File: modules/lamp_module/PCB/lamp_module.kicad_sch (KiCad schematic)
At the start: 36 parts, among them J1 Screw_Terminal_01x02, J2 Screw_Terminal_01x02, J3 Conn_01x06_Socket, K1 12V 5A, K2 12V 5A, Q1 2N7002H, Q2 2N7002H, U1 AMS1117-3.3, U2 ESP-12E, U4 PC817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

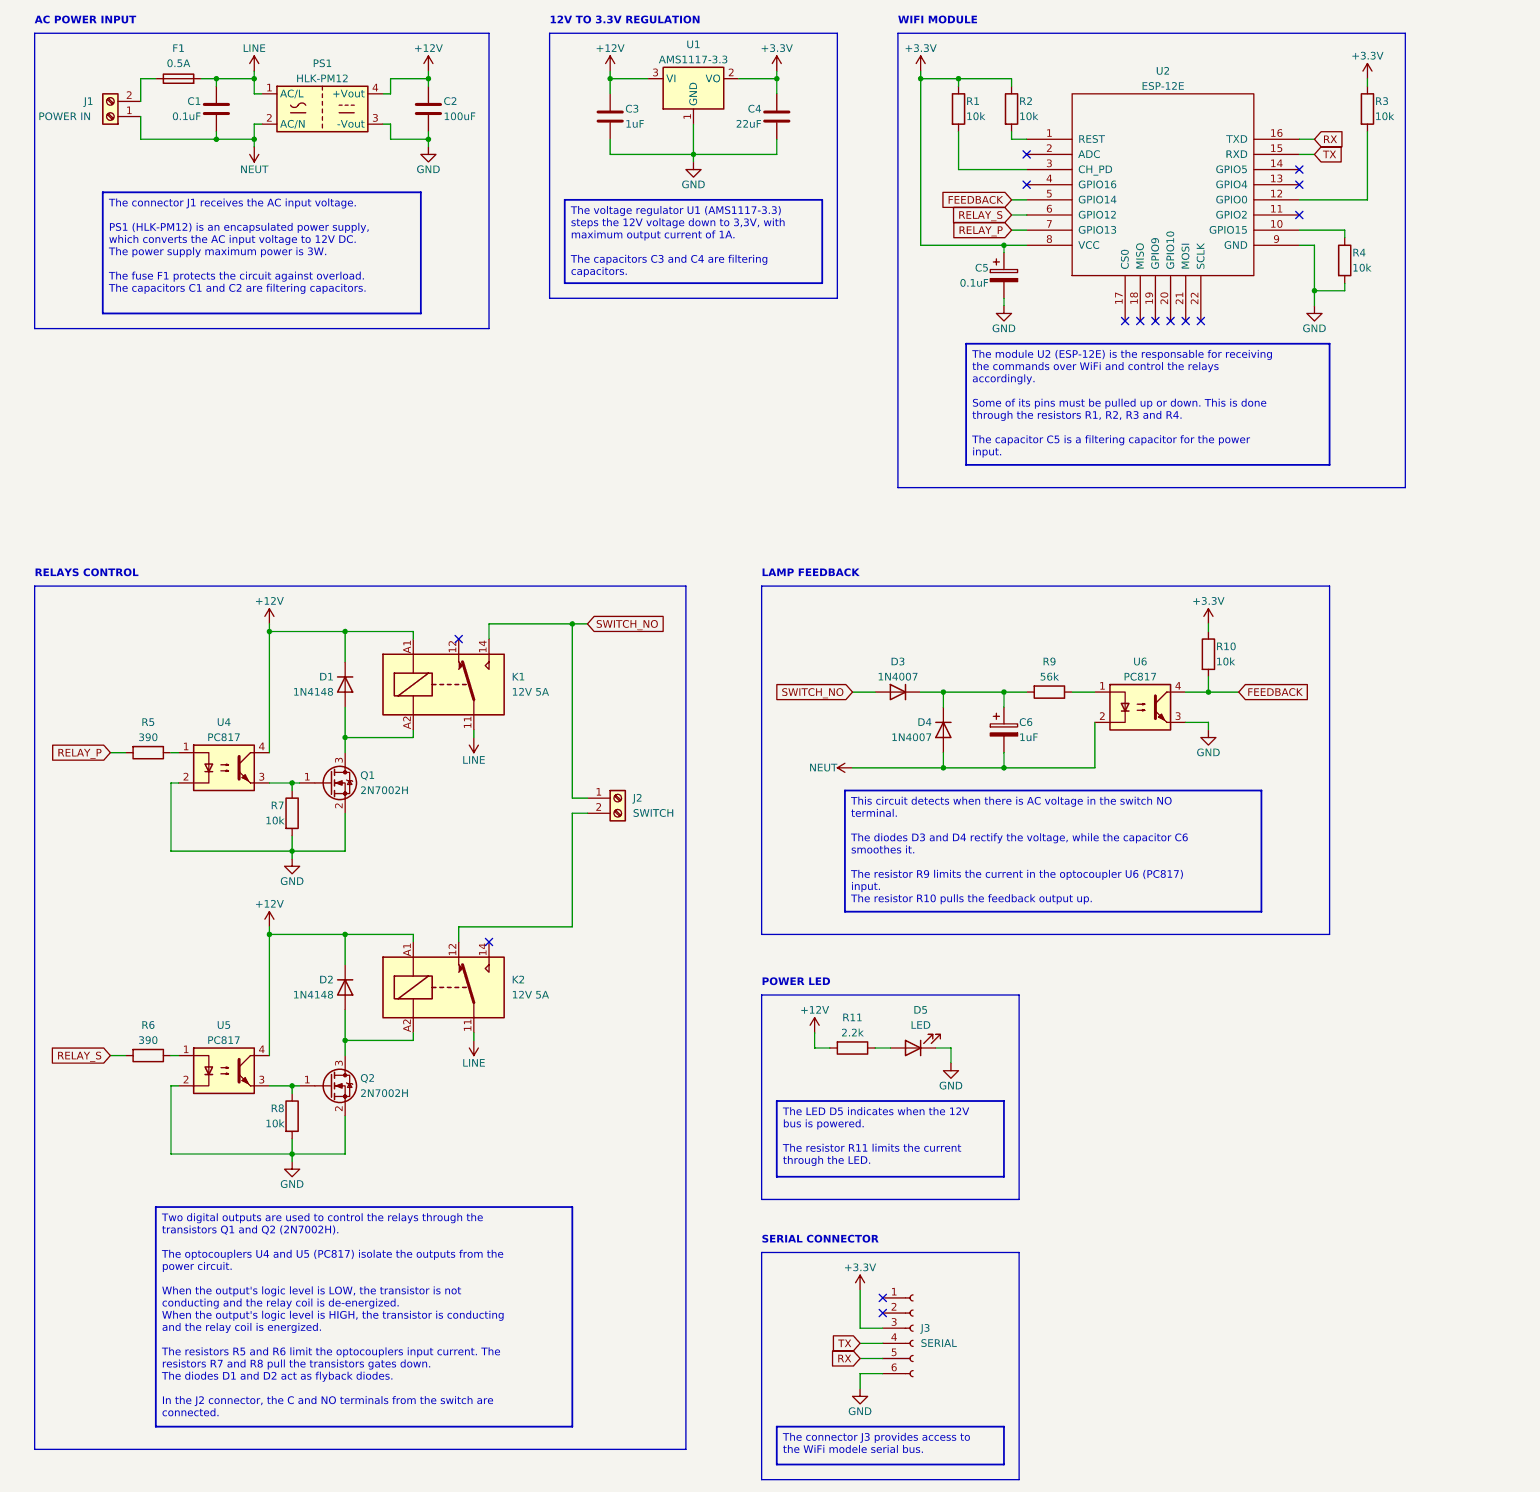
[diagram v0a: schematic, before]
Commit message: PCB simplified and improved
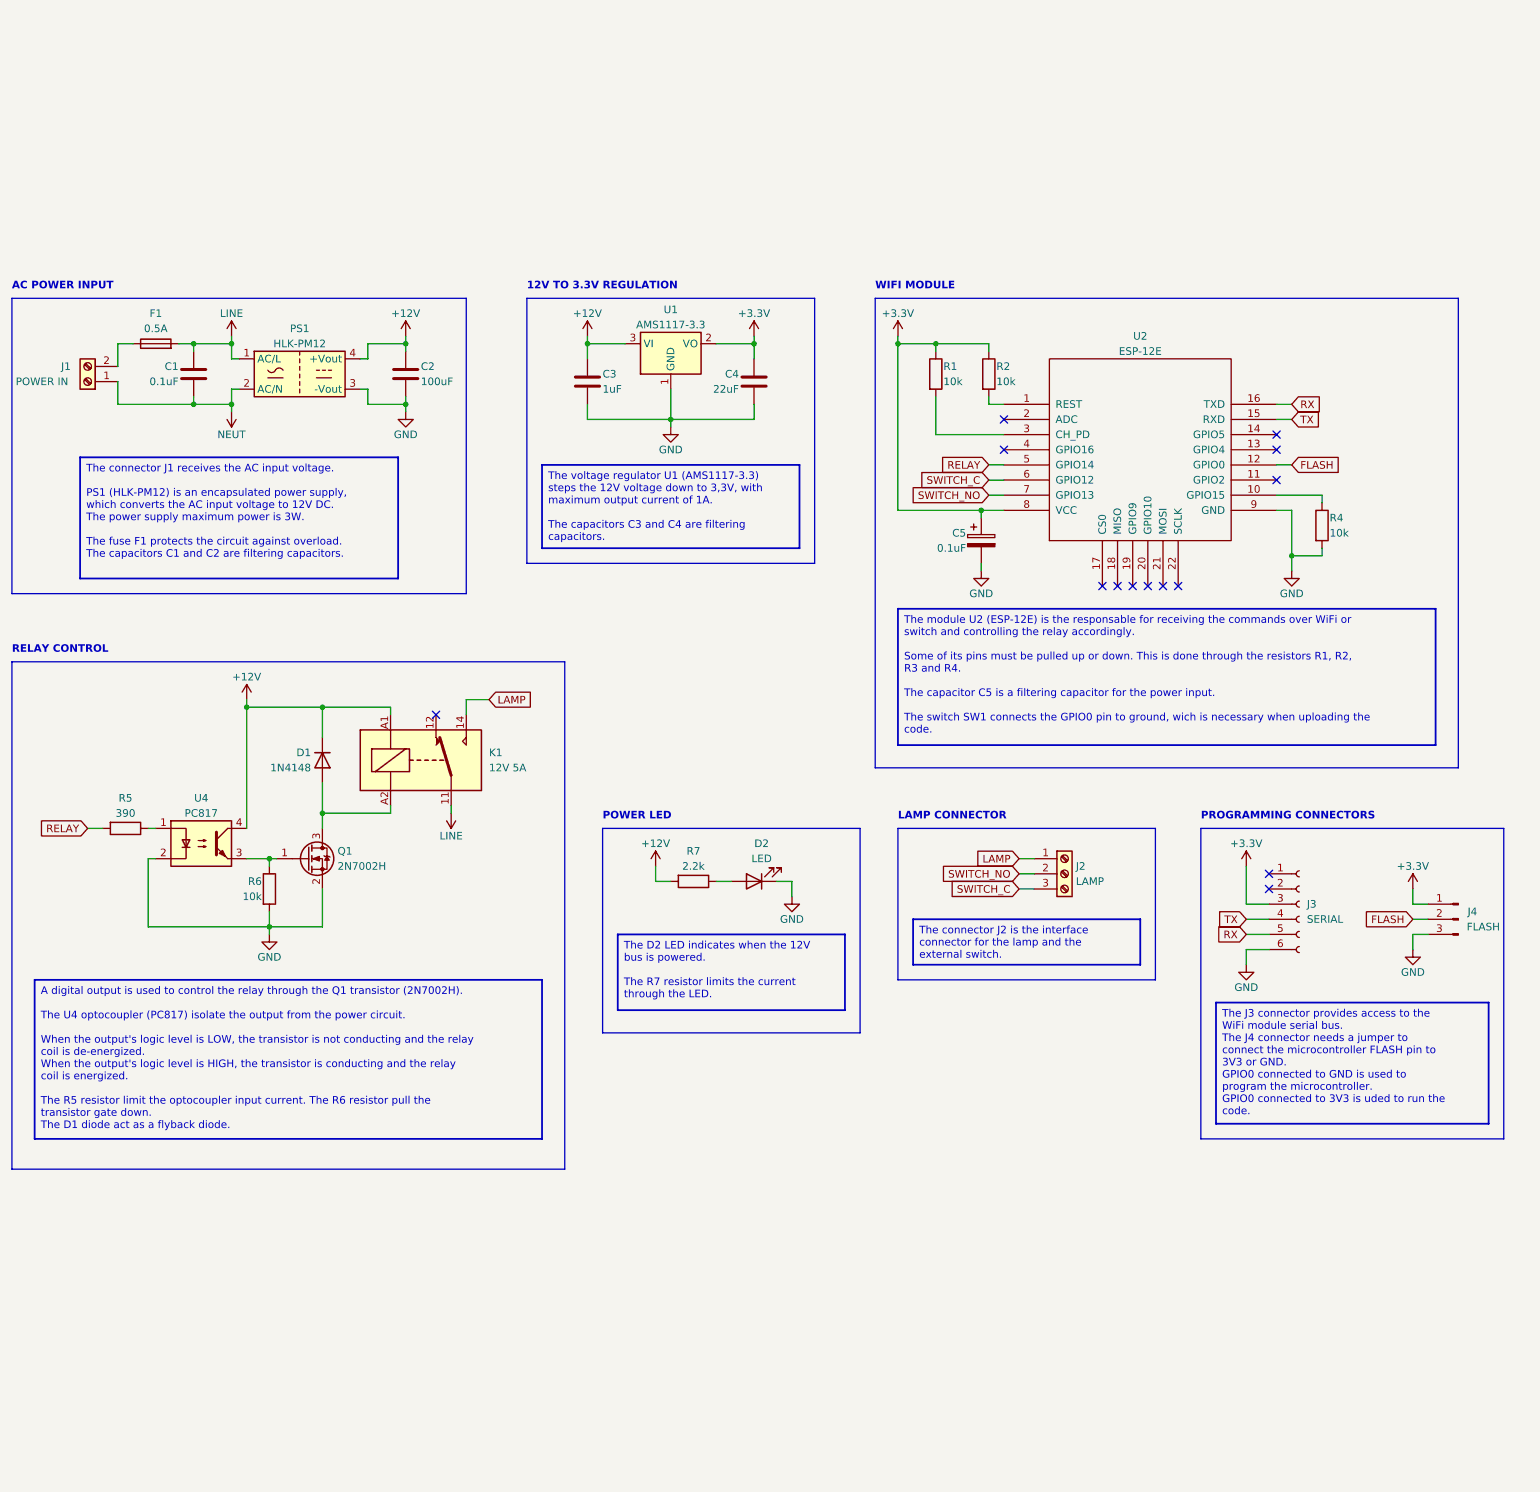
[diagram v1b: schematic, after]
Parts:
- removed C6: 1uF, Capacitor_THT:CP_Radial_D8.0mm_P3.50mm, symbol Device:C_Polarized
- removed D2: 1N4148, Diode_SMD:D_SOD-323F, symbol Diode:1N4148
- removed D3, D4: 1N4007, Diode_SMD:D_SMA, symbol Diode:1N4007
- removed J2: Screw_Terminal_01x02, TerminalBlock:TerminalBlock_bornier-2_P5.08mm, symbol Connector:Screw_Terminal_01x02
- removed K2: 12V 5A, Relay_THT:Relay_SPDT_Finder_36.11, symbol Relay:FINDER-36.11
- removed Q2: 2N7002H, Package_TO_SOT_SMD:SOT-23, symbol Transistor_FET:2N7002H
- removed R10, R3, R8: 10k, Resistor_SMD:R_0603_1608Metric, symbol Device:R
- removed R6: 390, Resistor_SMD:R_0603_1608Metric, symbol Device:R
- removed R9: 56k, Resistor_THT:R_Axial_DIN0309_L9.0mm_D3.2mm_P12.70mm_Horizontal, symbol Device:R
- removed U5, U6: PC817, Package_DIP:SMDIP-4_W7.62mm, symbol Isolator:PC817
- added J2: Screw_Terminal_01x03, TerminalBlock_Phoenix:TerminalBlock_Phoenix_MKDS-1,5-3-5.08_1x03_P5.08mm_Horizontal, symbol Connector:Screw_Terminal_01x03
- added J4: Conn_01x03_Socket, Connector_PinSocket_2.54mm:PinSocket_1x03_P2.54mm_Vertical, symbol Connector:Conn_01x03_Pin
- C1: footprint Capacitor_THT:C_Rect_L18.0mm_W8.0mm_P15.00mm_FKS3_FKP3 -> Capacitor_THT:C_Rect_L18.0mm_W6.0mm_P15.00mm_FKS3_FKP3
- J1: footprint TerminalBlock:TerminalBlock_bornier-2_P5.08mm -> TerminalBlock_Phoenix:TerminalBlock_Phoenix_MKDS-1,5-2-5.08_1x02_P5.08mm_Horizontal
- renumbered D5 to D2, R7 to R6, R11 to R7
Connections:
- net +3.3V: now also J4.1 (Pin_1)
- net GND: now also J4.3 (Pin_3)
- net SWITCH_NO: now also U2.7 (GPIO13), J2.2 (Pin_2); no longer K1.14
- net FLASH: now reaches U2.12 (GPIO0)
- net FLASH: now also J4.2 (Pin_2)
- net FEEDBACK renamed RELAY
- net RELAY: now also R5.2
- removed net RELAY_P: R5.2, U2.7 (GPIO13)
- net RELAY_S renamed SWITCH_C
- net SWITCH_C: now also J2.3 (Pin_3)
- new net LAMP: J2.1 (Pin_1), K1.14
- no-connect marks 15 -> 14
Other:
- note added: "LAMP CONNECTOR"
- note added: "PROGRAMMING CONNECTORS"
- note added: "RELAY CONTROL"
- note removed: "LAMP FEEDBACK"
- note removed: "RELAYS CONTROL"
- note removed: "SERIAL CONNECTOR"
- title: Lamp Module -> Lamp Module X1
- moved on the sheet: C1, C2, C3, C4, C5, D1, D2, F1, J1, J3, K1, PS1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
